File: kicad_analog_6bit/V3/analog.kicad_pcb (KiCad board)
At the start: 2 copper layers, 50 x 23.2 mm, 35 parts, among them P1 Conn_02x06_Odd_Even, P2 Conn_01x04, P3 Conn_01x06, P6 Conn_01x01, P7 Conn_01x01, U1 MAX9108, U2 MAX9108, U3 TS12A44514DR, U4 MAX5259EEE+, U5 MCP1754S-3302xCB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

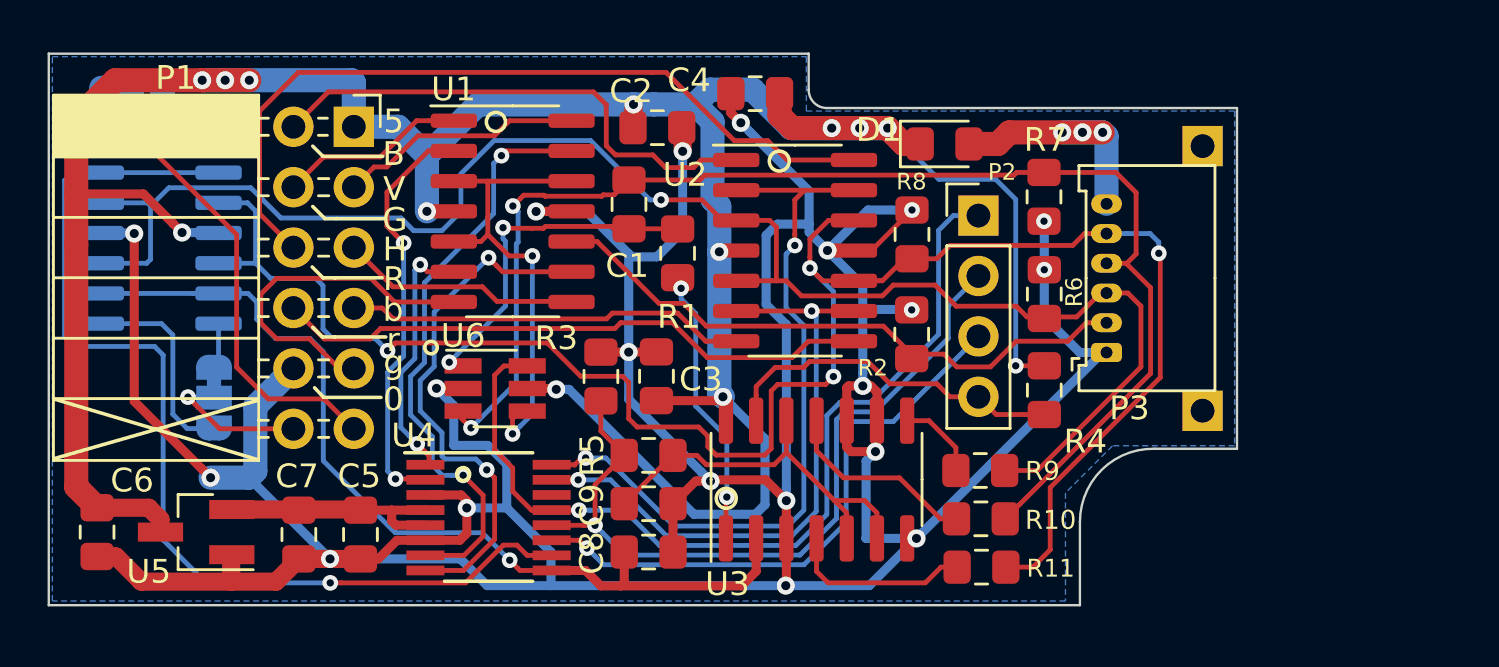
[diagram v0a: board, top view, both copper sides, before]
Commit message: Add IDC header for analog input
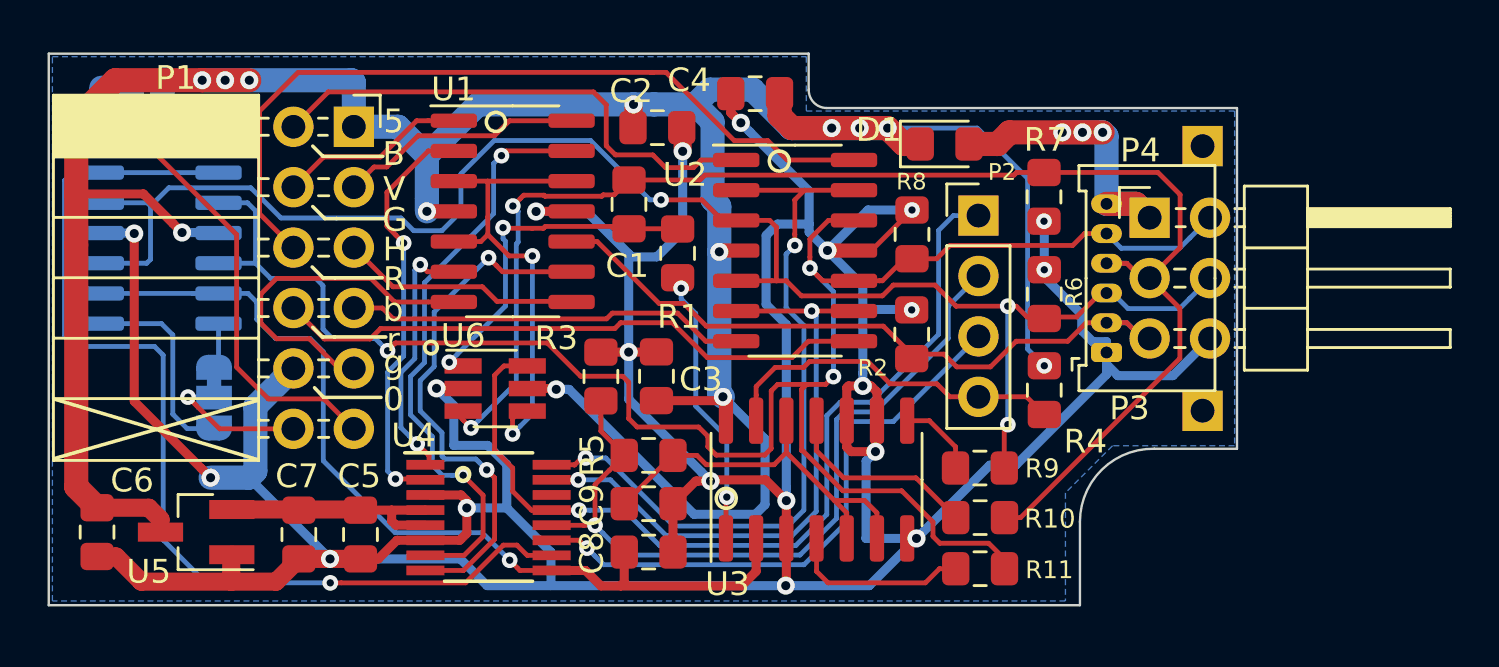
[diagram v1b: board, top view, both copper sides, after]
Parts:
- added P4: Conn_02x03_Odd_Even, Connector_PinHeader_2.54mm:PinHeader_2x03_P2.54mm_Horizontal, F.Cu at (73.8, 38.2)
- moved R9 0.11 mm to (66.7, 48.7)
- moved R11 0.09 mm to (66.7, 53.0)
- moved R10 0.06 mm to (66.7, 50.8)
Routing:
- net /AGREEN: track 56.0 -> 62.5 mm
- net /GND: track 197.5 -> 203.5 mm
- net /ASYNC: track 25.7 -> 29.9 mm
- net /VCC_IN: track 10.6 -> 14.7 mm
- net /ABLUE: track 68.4 -> 69.1 mm, vias 1 -> 3
- net /ARED: track 79.7 -> 79.8 mm, vias 4 -> 3

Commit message: Update V3
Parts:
- added P5: Conn_01x03_EVEN, Connector_Harwin:Harwin_M20-89003xx_1x03_P2.54mm_Horizontal_Custom_EVEN, F.Cu at (85.7, 39.0)
- D1: footprint Diode_SMD:D_0805_2012Metric_Pad1.15x1.40mm_HandSolder -> Diode_SMD:D_SOD-123
- P4: value Conn_02x03_Odd_Even -> Conn_01x03_ODD; footprint Connector_PinHeader_2.54mm:PinHeader_2x03_P2.54mm_Horizontal -> Connector_Harwin:Harwin_M20-89003xx_1x03_P2.54mm_Horizontal_Custom_ODD; moved to B.Cu
- moved P4 11.9 mm to (85.7, 39.0)
- moved P7 2.39 mm to (76.0, 32.8), turned to 270 degrees
- moved D1 0.34 mm to (65.5, 35.0)
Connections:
- net /UV1 renamed /X1
- net /UV2 renamed /X2
- P4 pad 1: /VCC_IN -> /GND
- P4 pad 3: /AGREEN -> /ABLUE
- P4 pad 5: /ASYNC -> /ARED
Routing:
- net /GND: track 203.5 -> 208.0 mm
- net /ASYNC: track 29.9 -> 34.3 mm
- net /ABLUE: track 69.1 -> 73.2 mm
- net /ARED: track 79.8 -> 83.8 mm
- net /VCC_IN: track 14.7 -> 18.4 mm
- net /AGREEN: track 62.5 -> 63.9 mm, vias 2 -> 4
- net /VCC: track 129.1 -> 128.4 mm
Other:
- board size 50 x 23.2 mm -> 54.4 x 23.2 mm
- board text added: "Fit 'P3' or 'P4'"
- board text added: "Pin 1"
- board text added: "X1"
- board text added: "X2"

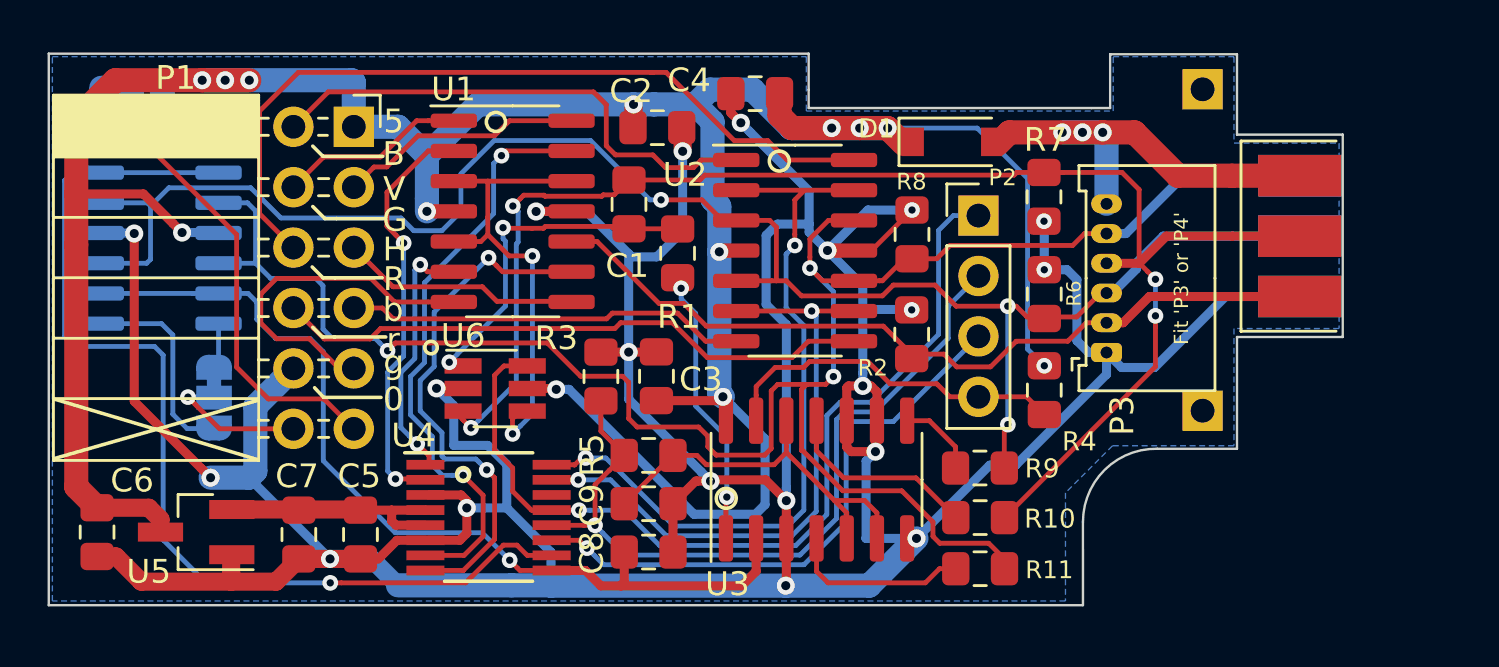
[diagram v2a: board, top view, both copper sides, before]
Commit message: Update V3 analog interface with 6 way IDC support.
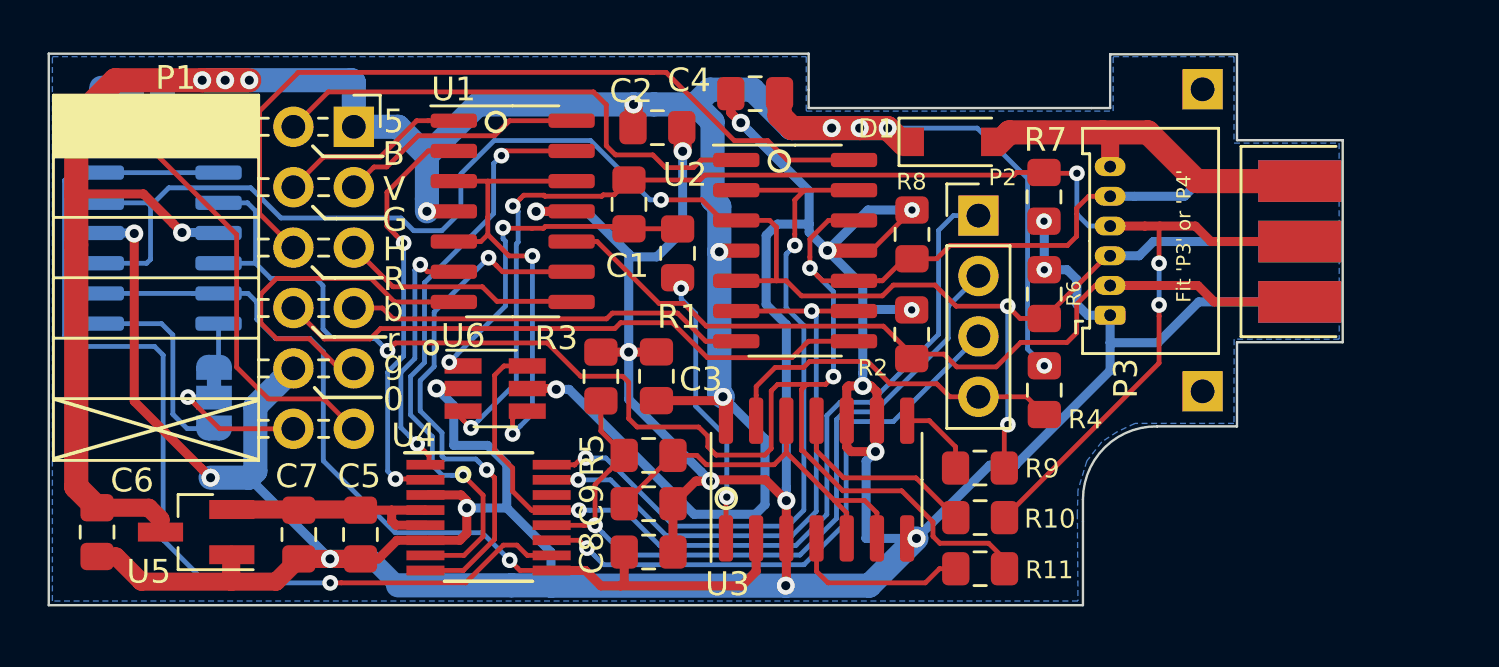
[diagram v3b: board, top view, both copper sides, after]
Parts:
- moved P3 1.57 mm to (72.2, 42.3)
- moved P6 0.81 mm to (76.0, 45.5)
- moved P4 0.23 mm to (85.7, 39.2)
- moved P5 0.23 mm to (85.7, 39.2)
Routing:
- net /VCC_IN: track 18.4 -> 15.5 mm, vias 3 -> 0
- net /AGREEN: track 63.9 -> 62.1 mm, vias 4 -> 5
- net /ASYNC: track 34.3 -> 35.5 mm
- net /GND: track 208.0 -> 207.3 mm
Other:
- outline, holes or cut-outs redrawn

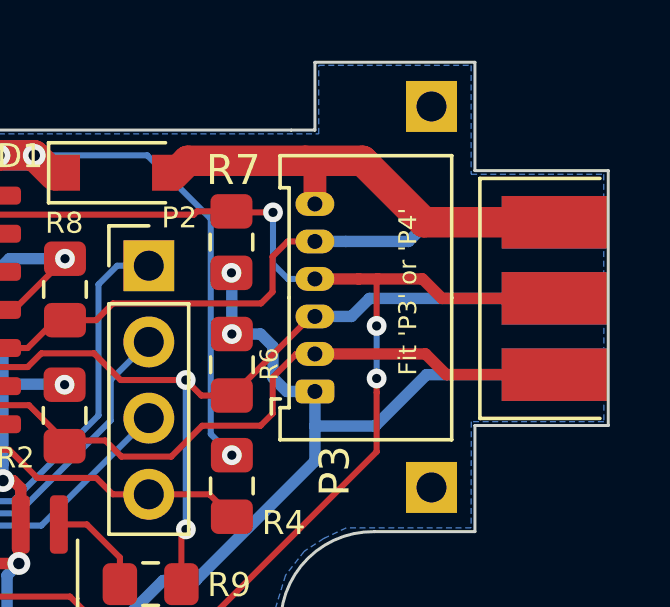
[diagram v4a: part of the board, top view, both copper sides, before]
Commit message: Update analog V3 board
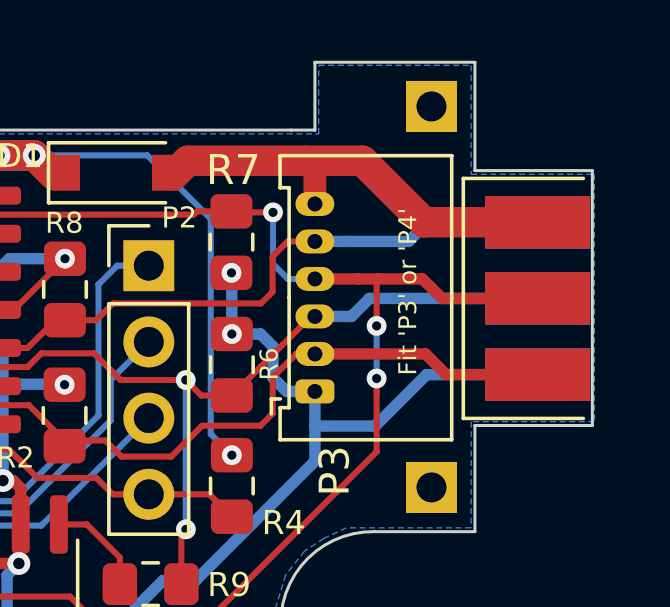
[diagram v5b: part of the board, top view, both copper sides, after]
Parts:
- R1: value 75R -> 100R
- moved P4 0.55 mm to (85.1, 39.2)
- moved P5 0.55 mm to (85.1, 39.2)
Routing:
- net /VCC_IN: track 15.5 -> 14.9 mm
- net /GND: track 207.3 -> 206.8 mm
- net /ARED: track 84.2 -> 83.6 mm
- net /AGREEN: track 62.1 -> 61.5 mm
- net /ABLUE: track 73.0 -> 72.4 mm
- net /ASYNC: track 35.5 -> 34.9 mm
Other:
- board size 54.4 x 23.2 mm -> 53.9 x 23.2 mm
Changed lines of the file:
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@@
       (effects (font (size 1 1) (thickness 0.15)))
     )
-    (fp_text value 75R (at 0 1.65 90) (layer F.Fab)
+    (fp_text value 100R (at 0 1.65 90) (layer F.Fab)
       (effects (font (size 1 1) (thickness 0.15)))
     )
@@
   )
   (module Connector_Harwin:Harwin_M20-89003xx_1x03_P2.54mm_Horizontal_Custom_EVEN (layer F.Cu)
-    (at 85.6552 39.20096)
+    (at 85.102 39.20096)
     (descr "Harwin Male Horizontal Surface Mount Single Row 2.54mm (0.1 inch) Pitch PCB Connector, M20-89003xx, 3 Pins per row (https://cdn.harwin.com/pdfs/M20-890.pdf), generated with kicad-footprint-generator")
     (tags "connector Harwin M20-890 horizontal")
@@
   )
   (module Connector_Harwin:Harwin_M20-89003xx_1x03_P2.54mm_Horizontal_Custom_ODD (layer B.Cu)
-    (at 85.6552 39.20096)
+    (at 85.102 39.20096)
     (descr "Harwin Male Horizontal Surface Mount Single Row 2.54mm (0.1 inch) Pitch PCB Connector, M20-89003xx, 3 Pins per row (https://cdn.harwin.com/pdfs/M20-890.pdf), generated with kicad-footprint-generator")
     (tags "connector Harwin M20-890 horizontal")
@@
     )
   )
+  (gr_line (start 77.4886 43.43654) (end 81.402 43.43654) (layer Edge.Cuts) (width 0.1))
+  (gr_line (start 77.4886 34.94024) (end 81.402 34.94024) (layer Edge.Cuts) (width 0.1))
   (gr_line (start 77.4886 31.32836) (end 77.4886 34.94024) (layer Edge.Cuts) (width 0.1))
-  (gr_line (start 81.9336 34.94024) (end 81.9336 43.43654) (layer Edge.Cuts) (width 0.1))
+  (gr_line (start 81.402 34.94024) (end 81.402 43.43654) (layer Edge.Cuts) (width 0.1))
   (gr_line (start 77.4886 43.43654) (end 77.4886 46.97476) (layer Edge.Cuts) (width 0.1))
-  (gr_line (start 81.9336 43.43654) (end 77.4886 43.43654) (layer Edge.Cuts) (width 0.1))
   (gr_line (start 74.135799 46.97476) (end 77.4886 46.97476) (layer Edge.Cuts) (width 0.1))
   (gr_line (start 71.011181 50.04816) (end 71.011181 50.987961) (layer Edge.Cuts) (width 0.1))
-  (gr_line (start 81.9336 34.94024) (end 77.4886 34.94024) (layer Edge.Cuts) (width 0.1))
   (gr_text X2 (at 40.2776 48.82896) (layer B.SilkS)
     (effects (font (size 0.8 0.8) (thickness 0.12)) (justify mirror))
@@
     (effects (font (size 0.8 0.8) (thickness 0.12)) (justify mirror))
   )
-  (gr_text "Pin 1" (at 75.9138 41.58996) (layer B.SilkS)
+  (gr_text "Pin 1" (at 75.68774 41.56456) (layer B.SilkS)
     (effects (font (size 0.6 0.6) (thickness 0.1)) (justify mirror))
   )
@@
   (segment (start 68.18735 48.60521) (end 68.18735 48.59251) (width 0.381) (layer B.Cu) (net 1))
   (segment (start 68.18735 48.59251) (end 72.1546 44.62526) (width 0.381) (layer B.Cu) (net 1))
+  (segment (start 72.1546 44.62526) (end 72.1546 43.45686) (width 0.381) (layer B.Cu) (net 1))
+  (segment (start 72.1546 43.45686) (end 72.1546 42.30096) (width 0.381) (layer B.Cu) (net 1))
   (segment (start 74.1612 43.45686) (end 72.1546 43.45686) (width 0.381) (layer B.Cu) (net 1))
   (segment (start 75.8771 41.74096) (end 74.1612 43.45686) (width 0.381) (layer B.Cu) (net 1))
-  (segment (start 80.1302 41.74096) (end 75.8771 41.74096) (width 0.381) (layer B.Cu) (net 1))
-  (segment (start 72.1546 44.62526) (end 72.1546 43.45686) (width 0.381) (layer B.Cu) (net 1))
-  (segment (start 72.1546 43.45686) (end 72.1546 42.30096) (width 0.381) (layer B.Cu) (net 1))
+  (segment (start 79.577 41.74096) (end 75.8771 41.74096) (width 0.381) (layer B.Cu) (net 1))
   (segment (start 42.00226 41.10482) (end 40.3538 39.45636) (width 0.2032) (layer F.Cu) (net 2))
   (segment (start 45.75892 41.10482) (end 42.00226 41.10482) (width 0.2032) (layer F.Cu) (net 2))
@@
   (segment (start 41.945 50.95356) (end 42.1191 51.12766) (width 0.381) (layer F.Cu) (net 10))
   (segment (start 72.1546 40.84796) (end 72.4046 40.84796) (width 0.381) (layer F.Cu) (net 11))
-  (segment (start 75.84216 41.05096) (end 72.1546 41.05096) (width 0.381) (layer F.Cu) (net 11))
-  (segment (start 76.53216 41.74096) (end 75.84216 41.05096) (width 0.381) (layer F.Cu) (net 11))
-  (segment (start 80.1302 41.74096) (end 76.53216 41.74096) (width 0.381) (layer F.Cu) (net 11))
   (segment (start 71.53028 41.05096) (end 72.1546 41.05096) (width 0.2032) (layer F.Cu) (net 11))
   (segment (start 70.74744 41.8338) (end 71.53028 41.05096) (width 0.2032) (layer F.Cu) (net 11))
@@
   (segment (start 49.509 39.20236) (end 50.584 39.20236) (width 0.2032) (layer F.Cu) (net 11))
   (segment (start 62.6206 42.75836) (end 63.798 43.93576) (width 0.2032) (layer F.Cu) (net 11))
+  (segment (start 75.84216 41.05096) (end 72.1546 41.05096) (width 0.381) (layer F.Cu) (net 11))
+  (segment (start 79.577 41.74096) (end 76.53216 41.74096) (width 0.381) (layer F.Cu) (net 11))
+  (segment (start 76.53216 41.74096) (end 75.84216 41.05096) (width 0.381) (layer F.Cu) (net 11))
   (segment (start 59.530809 39.091051) (end 59.530809 39.852996) (width 0.2032) (layer F.Cu) (net 12))
   (segment (start 61.3835 40.85336) (end 60.0642 40.85336) (width 0.2032) (layer F.Cu) (net 12))
@@
   (segment (start 73.1856 37.30096) (end 72.1546 37.30096) (width 0.381) (layer B.Cu) (net 12))
   (segment (start 75.2752 37.30096) (end 73.1856 37.30096) (width 0.381) (layer B.Cu) (net 12))
-  (segment (start 80.1302 36.66096) (end 75.9152 36.66096) (width 0.381) (layer B.Cu) (net 12))
   (segment (start 75.9152 36.66096) (end 75.2752 37.30096) (width 0.381) (layer B.Cu) (net 12))
+  (segment (start 79.577 36.66096) (end 75.9152 36.66096) (width 0.381) (layer B.Cu) (net 12))
   (segment (start 50.7805 37.29736) (end 48.390513 37.29736) (width 0.2032) (layer F.Cu) (net 13))
   (via (at 47.040402 37.709336) (size 0.6604) (drill 0.3048) (layers F.Cu B.Cu) (net 13))
@@
   (segment (start 74.2464 38.55096) (end 73.61648 38.55096) (width 0.381) (layer F.Cu) (net 13))
   (segment (start 75.73992 38.55096) (end 74.2464 38.55096) (width 0.381) (layer F.Cu) (net 13))
-  (segment (start 80.1302 39.20096) (end 76.38992 39.20096) (width 0.381) (layer F.Cu) (net 13))
+  (segment (start 79.577 39.20096) (end 76.38992 39.20096) (width 0.381) (layer F.Cu) (net 13))
   (segment (start 76.38992 39.20096) (end 75.73992 38.55096) (width 0.381) (layer F.Cu) (net 13))
   (via (at 53.27224 37.44976) (size 0.6604) (drill 0.3048) (layers F.Cu B.Cu) (net 14))
@@
   (segment (start 67.8493 41.92016) (end 68.3663 42.43716) (width 0.2032) (layer F.Cu) (net 14))
   (segment (start 71.9046 39.59796) (end 72.1546 39.59796) (width 0.2032) (layer F.Cu) (net 14))
-  (segment (start 73.3721 39.80096) (end 72.1546 39.80096) (width 0.381) (layer B.Cu) (net 14))
-  (segment (start 80.1302 39.20096) (end 73.9721 39.20096) (width 0.381) (layer B.Cu) (net 14))
-  (segment (start 73.9721 39.20096) (end 73.3721 39.80096) (width 0.381) (layer B.Cu) (net 14))
   (segment (start 69.386 42.43716) (end 72.0222 39.80096) (width 0.2032) (layer F.Cu) (net 14))
   (segment (start 72.0222 39.80096) (end 72.1546 39.80096) (width 0.2032) (layer F.Cu) (net 14))
+  (segment (start 73.3721 39.80096) (end 72.1546 39.80096) (width 0.381) (layer B.Cu) (net 14))
+  (segment (start 73.9721 39.20096) (end 73.3721 39.80096) (width 0.381) (layer B.Cu) (net 14))
+  (segment (start 79.577 39.20096) (end 73.9721 39.20096) (width 0.381) (layer B.Cu) (net 14))
   (via (at 46.019561 39.883148) (size 0.6604) (drill 0.3048) (layers F.Cu B.Cu) (net 16))
   (segment (start 46.34976 40.213347) (end 46.019561 39.883148) (width 0.2032) (layer F.Cu) (net 16))
@@
   (segment (start 72.1546 36.05096) (end 72.1546 34.68596) (width 0.762) (layer F.Cu) (net 30))
   (segment (start 72.1546 34.68596) (end 72.1038 34.63516) (width 0.762) (layer F.Cu) (net 30))
-  (segment (start 75.79048 36.66096) (end 80.1302 36.66096) (width 1.016) (layer F.Cu) (net 30))
-  (segment (start 71.83964 34.61258) (end 73.7421 34.61258) (width 1.016) (layer F.Cu) (net 30))
-  (segment (start 73.7421 34.61258) (end 75.79048 36.66096) (width 1.016) (layer F.Cu) (net 30))
+  (segment (start 73.7421 34.61258) (end 71.83964 34.61258) (width 1.016) (layer F.Cu) (net 30))
+  (segment (start 75.79048 36.66096) (end 73.7421 34.61258) (width 1.016) (layer F.Cu) (net 30))
+  (segment (start 75.79048 36.66096) (end 79.577 36.66096) (width 1.016) (layer F.Cu) (net 30))
   (via (at 39.3632 53.55336) (size 0.6604) (drill 0.3048) (layers F.Cu B.Cu) (net 31))
   (segment (start 39.5283 53.71846) (end 39.3632 53.55336) (width 0.2032) (layer F.Cu) (net 31))
@@
       (pts
         (xy 27.6792 31.42996) (xy 59.3784 31.42996) (xy 59.3784 33.71596) (xy 72.2816 33.71596) (xy 72.2816 31.42996)
-        (xy 77.3616 31.42996) (xy 77.3616 35.06216) (xy 81.7812 35.06216) (xy 81.78628 43.307) (xy 77.36668 43.307)
+        (xy 77.3616 31.42996) (xy 77.3616 35.06216) (xy 81.46878 35.06216) (xy 81.472 43.307) (xy 77.36668 43.307)
         (xy 77.3616 46.84776) (xy 73.202 46.84776) (xy 72.452 47.20096) (xy 71.802 47.62596) (xy 71.177 48.42596)
         (xy 70.802 49.65096) (xy 70.777 50.62596) (xy 70.802 54.31536) (xy 27.6792 54.31536)
@@
     (polygon
       (pts
-        (xy 81.49928 39.75608) (xy 81.49928 40.87368) (xy 73.32048 40.87368) (xy 73.32048 39.75608)
+        (xy 81.335953 39.75608) (xy 81.335953 40.87368) (xy 73.157153 40.87368) (xy 73.157153 39.75608)
       )
     )
